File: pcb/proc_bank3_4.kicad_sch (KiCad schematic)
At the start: 2 parts, among them U1 XC6SLX16-FTG256

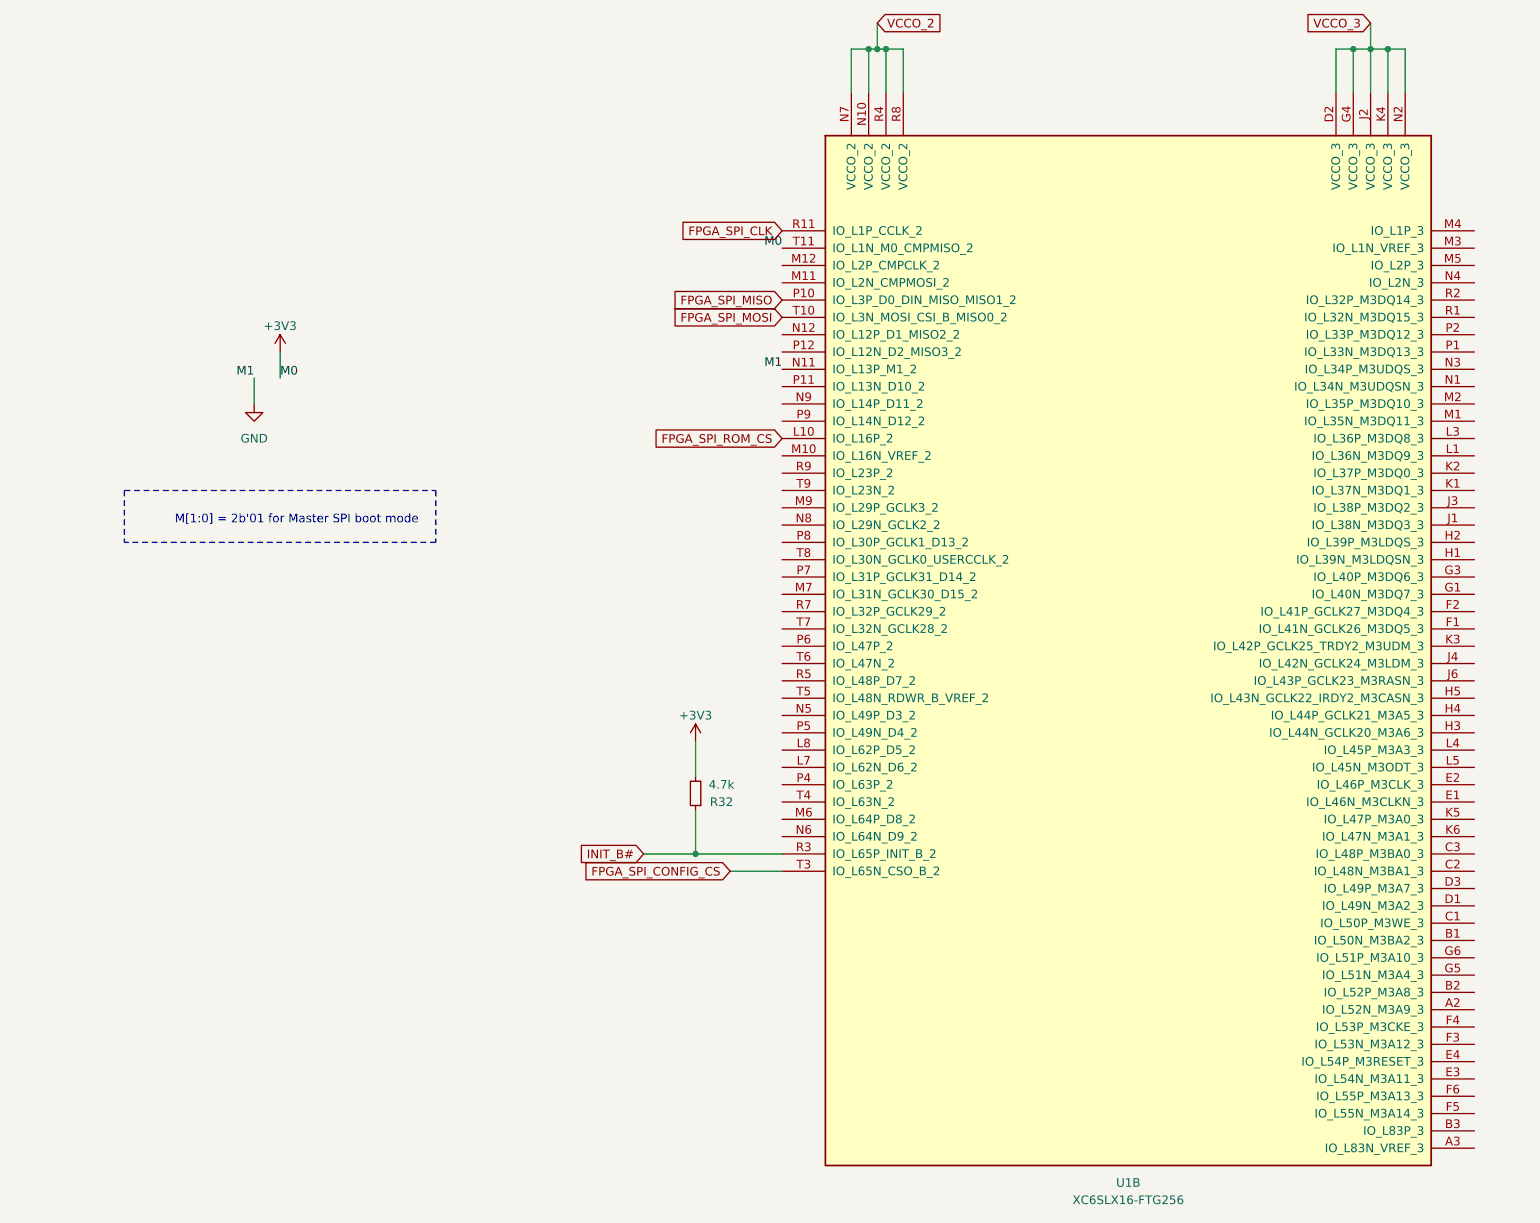
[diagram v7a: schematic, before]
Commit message: change to lx9 and reduce power
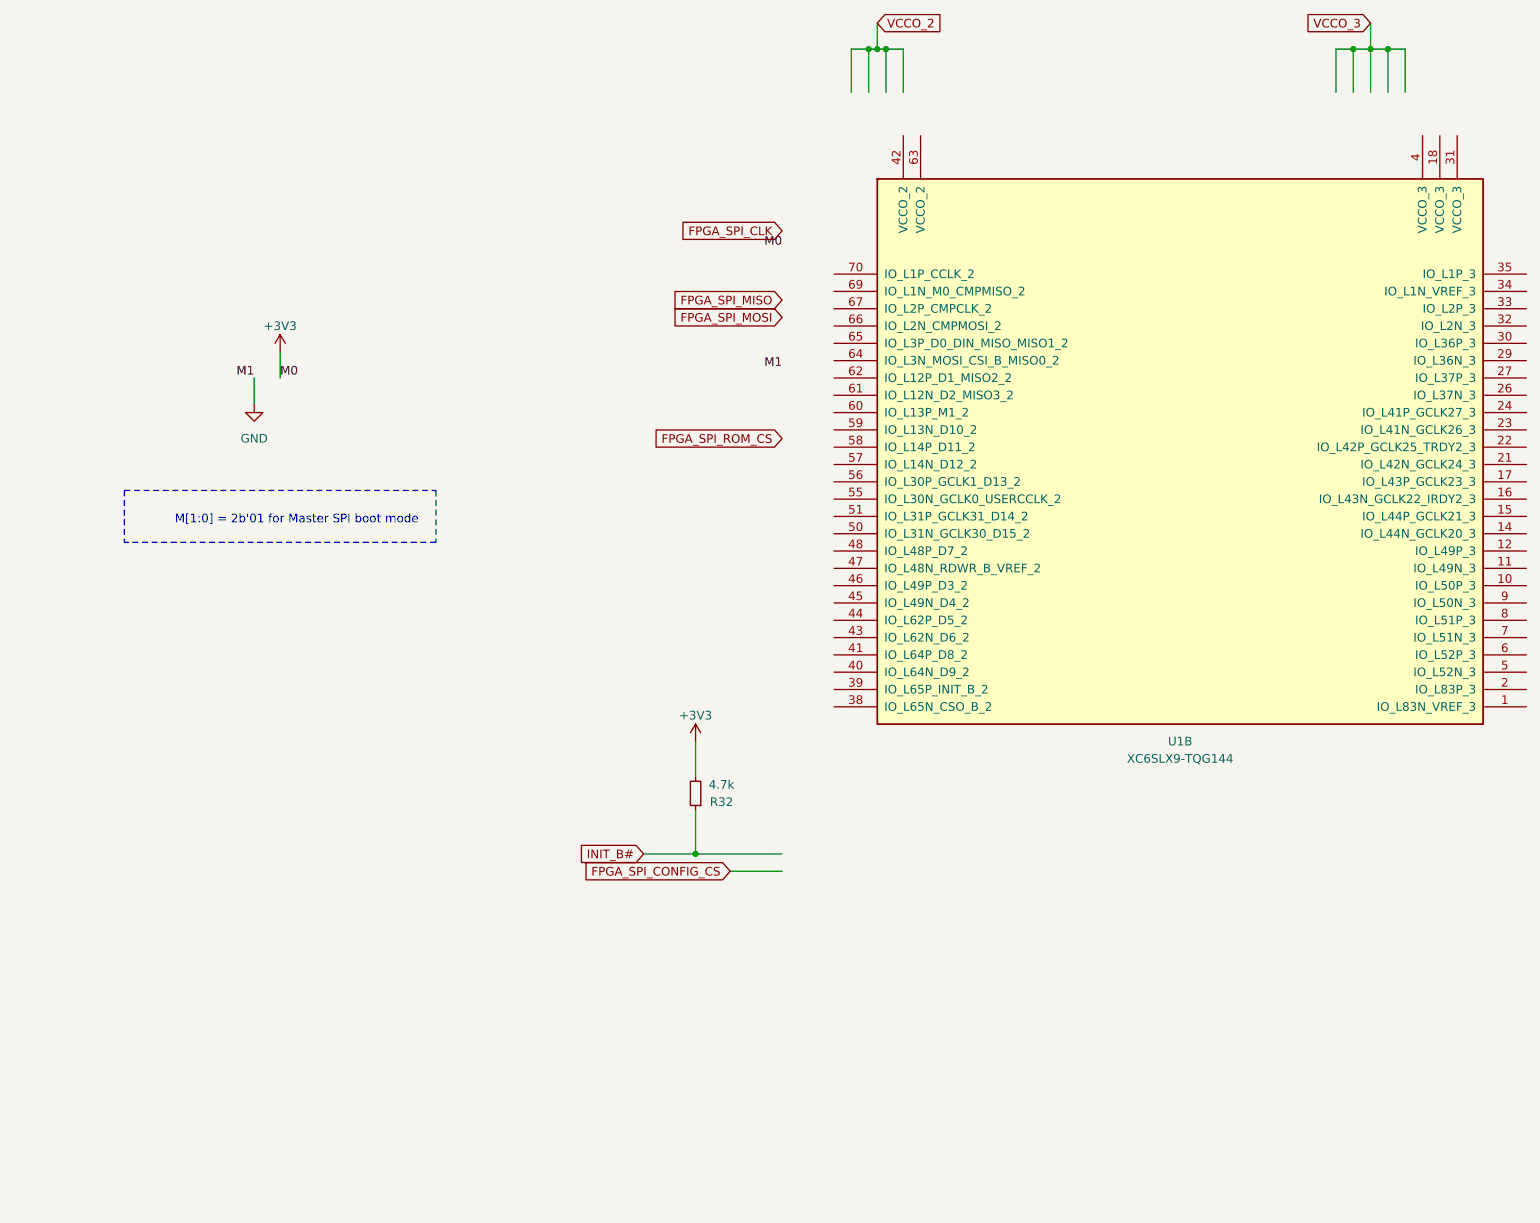
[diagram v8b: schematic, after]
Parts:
- removed U1: XC6SLX16-FTG256, Package_BGA:Xilinx_FTG256, symbol FPGA_Xilinx_Spartan6:XC6SLX16-FTG256
- added U1: XC6SLX9-TQG144, Package_QFP:TQFP-144_20x20mm_P0.5mm, symbol FPGA_Xilinx_Spartan6:XC6SLX9-TQG144
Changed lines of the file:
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@@
     (pin "2")
   )
-  (symbol (lib_id "FPGA_Xilinx_Spartan6:XC6SLX16-FTG256") (at 185.42 114.3 0) (unit 2)
+  (symbol (lib_id "FPGA_Xilinx_Spartan6:XC6SLX9-TQG144") (at 193.04 85.09 0) (unit 2)
     (in_bom yes) (on_board yes) (fields_autoplaced)
-    (property "Reference" "U1" (id 0) (at 185.42 195.58 0))
-    (property "Value" "XC6SLX16-FTG256" (id 1) (at 185.42 198.12 0))
-    (property "Footprint" "Package_BGA:Xilinx_FTG256" (id 2) (at 185.42 114.3 0)
+    (property "Reference" "U1" (id 0) (at 193.04 130.81 0))
+    (property "Value" "XC6SLX9-TQG144" (id 1) (at 193.04 133.35 0))
+    (property "Footprint" "Package_QFP:TQFP-144_20x20mm_P0.5mm" (id 2) (at 193.04 85.09 0)
       (effects (font (size 1.27 1.27)) hide)
     )
-    (property "Datasheet" "" (id 3) (at 185.42 114.3 0))
-    (pin "A2")
-    (pin "A3")
-    (pin "B1")
-    (pin "B2")
-    (pin "B3")
-    (pin "C1")
-    (pin "C2")
-    (pin "C3")
-    (pin "D1")
-    (pin "D2")
-    (pin "D3")
-    (pin "E1")
-    (pin "E2")
-    (pin "E3")
-    (pin "E4")
-    (pin "F1")
-    (pin "F2")
-    (pin "F3")
-    (pin "F4")
-    (pin "F5")
-    (pin "F6")
-    (pin "G1")
-    (pin "G3")
-    (pin "G4")
-    (pin "G5")
-    (pin "G6")
-    (pin "H1")
-    (pin "H2")
-    (pin "H3")
-    (pin "H4")
-    (pin "H5")
-    (pin "J1")
-    (pin "J2")
-    (pin "J3")
-    (pin "J4")
-    (pin "J6")
-    (pin "K1")
-    (pin "K2")
-    (pin "K3")
-    (pin "K4")
-    (pin "K5")
-    (pin "K6")
-    (pin "L1")
-    (pin "L10")
-    (pin "L3")
-    (pin "L4")
-    (pin "L5")
-    (pin "L7")
-    (pin "L8")
-    (pin "M1")
-    (pin "M10")
-    (pin "M11")
-    (pin "M12")
-    (pin "M2")
-    (pin "M3")
-    (pin "M4")
-    (pin "M5")
-    (pin "M6")
-    (pin "M7")
-    (pin "M9")
-    (pin "N1")
-    (pin "N10")
-    (pin "N11")
-    (pin "N12")
-    (pin "N2")
-    (pin "N3")
-    (pin "N4")
-    (pin "N5")
-    (pin "N6")
-    (pin "N7")
-    (pin "N8")
-    (pin "N9")
-    (pin "P1")
-    (pin "P10")
-    (pin "P11")
-    (pin "P12")
-    (pin "P2")
-    (pin "P4")
-    (pin "P5")
-    (pin "P6")
-    (pin "P7")
-    (pin "P8")
-    (pin "P9")
-    (pin "R1")
-    (pin "R11")
-    (pin "R2")
-    (pin "R3")
-    (pin "R4")
-    (pin "R5")
-    (pin "R7")
-    (pin "R8")
-    (pin "R9")
-    (pin "T10")
-    (pin "T11")
-    (pin "T3")
-    (pin "T4")
-    (pin "T5")
-    (pin "T6")
-    (pin "T7")
-    (pin "T8")
-    (pin "T9")
+    (property "Datasheet" "" (id 3) (at 193.04 85.09 0))
+    (pin "1")
+    (pin "10")
+    (pin "11")
+    (pin "12")
+    (pin "14")
+    (pin "15")
+    (pin "16")
+    (pin "17")
+    (pin "18")
+    (pin "2")
+    (pin "21")
+    (pin "22")
+    (pin "23")
+    (pin "24")
+    (pin "26")
+    (pin "27")
+    (pin "29")
+    (pin "30")
+    (pin "31")
+    (pin "32")
+    (pin "33")
+    (pin "34")
+    (pin "35")
+    (pin "38")
+    (pin "39")
+    (pin "4")
+    (pin "40")
+    (pin "41")
+    (pin "42")
+    (pin "43")
+    (pin "44")
+    (pin "45")
+    (pin "46")
+    (pin "47")
+    (pin "48")
+    (pin "5")
+    (pin "50")
+    (pin "51")
+    (pin "55")
+    (pin "56")
+    (pin "57")
+    (pin "58")
+    (pin "59")
+    (pin "6")
+    (pin "60")
+    (pin "61")
+    (pin "62")
+    (pin "63")
+    (pin "64")
+    (pin "65")
+    (pin "66")
+    (pin "67")
+    (pin "69")
+    (pin "7")
+    (pin "70")
+    (pin "8")
+    (pin "9")
   )
 )
